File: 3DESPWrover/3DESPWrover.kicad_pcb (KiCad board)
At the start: 2 copper layers, 40 x 40 mm, 21 parts, among them J1 Conn_01x05_Male, J2 Conn_01x03_Female, J3 Conn_02x03_Odd_Even, J4 Conn_02x07_Odd_Even, SW1 SW_Push, SW2 SW_Push, U1 ESP32-S2-WROVER

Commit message: Cleared Andres comments
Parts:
- added NT1: Net-Tie_2, NetTie:NetTie-2_SMD_Pad0.5mm, B.Cu at (231.1, 85.5)
- added R4: 10k, Resistor_SMD:R_0805_2012Metric_Pad1.20x1.40mm_HandSolder, F.Cu at (211.5, 81.7)
- moved J4 0.97 mm to (232.8, 59.8)
- moved SW2 0.76 mm to (205.1, 79.1)
- moved J2 0.38 mm to (231.3, 81.2)
- turned C8 to 180 degrees
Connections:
- J3 pad 2: /D6 -> GND
- J3 pad 3: /Vin -> /D6
- J3 pad 5: GND -> /Vin
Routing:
- net /D14: track 47.4 -> 38.8 mm
- net /D15: track 44.7 -> 36.1 mm
- net /D16: track 46.2 -> 38.3 mm
- net /D13: track 42.3 -> 36.5 mm
- net /D12: track 43.7 -> 38.3 mm
- net /D11: track 39.4 -> 34.3 mm
- net /AD1: track 0.00 -> 5.12 mm, vias 0 -> 1
- net /D8: track 37.7 -> 33.1 mm
- net /D9: track 36.6 -> 32.1 mm
- net /D10: track 40.0 -> 36.2 mm
- net +3V3: track 79.1 -> 82.7 mm
- net GND: track 10.6 -> 7.31 mm
- net /D6: track 2.32 -> 5.36 mm
- net /NEOPIX: track 46.2 -> 48.5 mm
- net /RESET: track 19.8 -> 21.9 mm
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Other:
- outline, holes or cut-outs redrawn

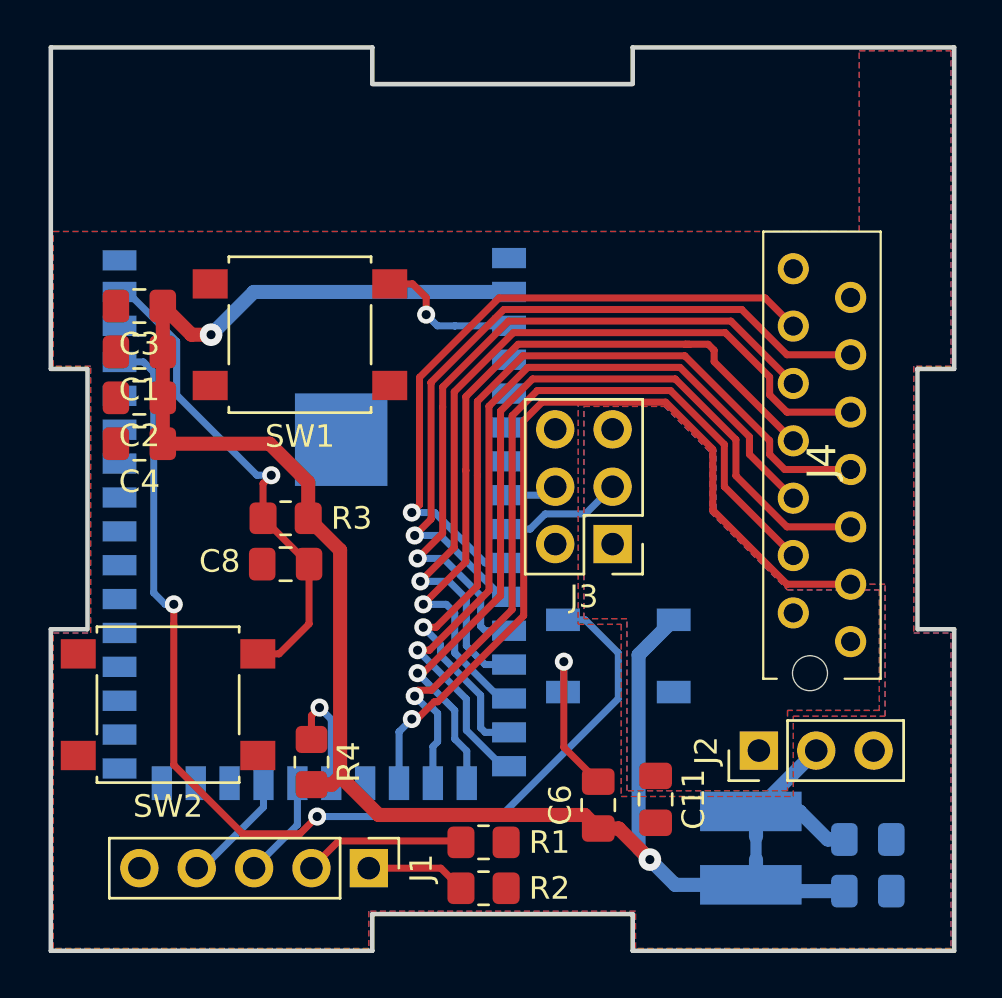
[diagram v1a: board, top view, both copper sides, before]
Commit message: Made corrections and added holes for zipties/nylon
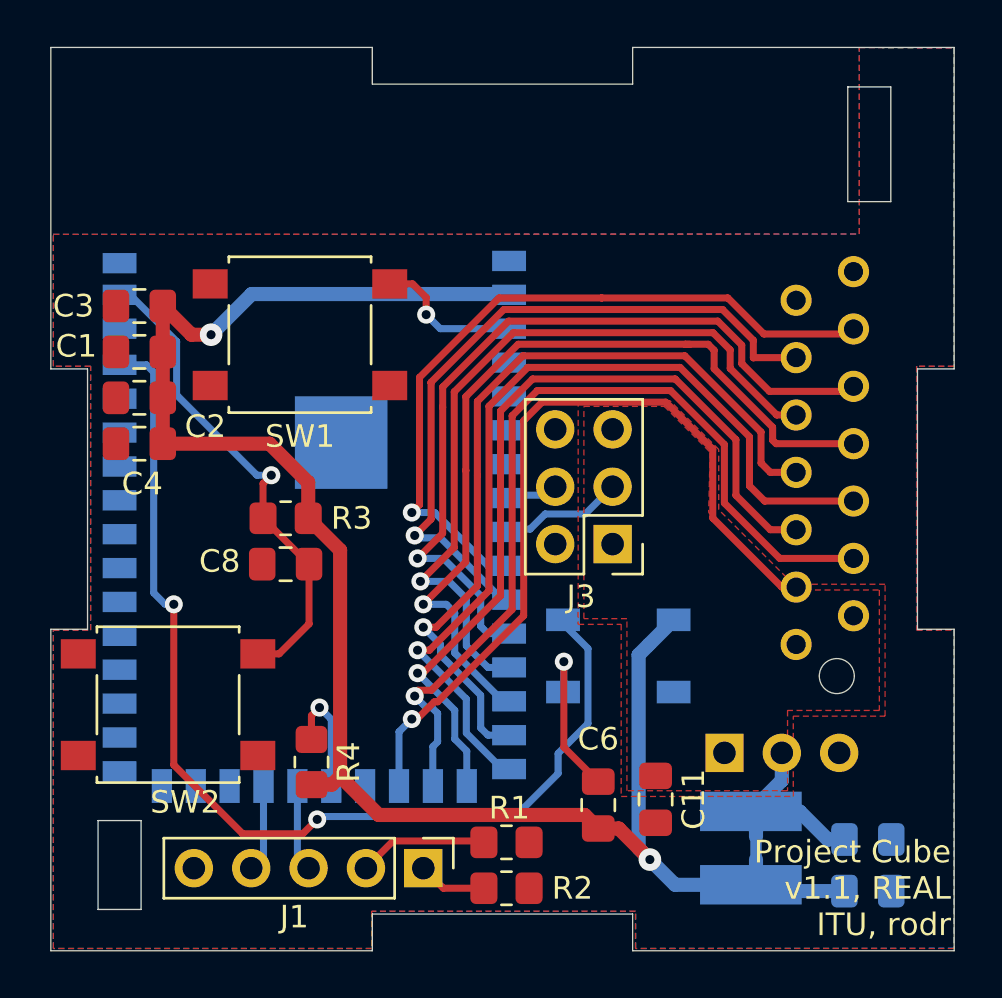
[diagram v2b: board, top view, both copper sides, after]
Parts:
- J2, J4: moved to B.Cu
- moved J4 2.67 mm to (235.5, 59.9)
- moved J1 2.41 mm to (216.4, 86.4)
- moved J2 1.53 mm to (229.7, 81.3), turned to 270 degrees
- moved R1 1.02 mm to (220.1, 85.2)
- moved R2 1.02 mm to (220.1, 87.2)
- moved U1 0.13 mm to (211.6, 71.2)
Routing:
- net /D13: track 36.5 -> 40.1 mm
- net /D9: track 32.1 -> 35.5 mm
- net /D11: track 34.3 -> 37.6 mm
- net /D15: track 36.1 -> 39.4 mm
- net /D7: track 29.9 -> 32.8 mm
- net /D10: track 36.2 -> 34.0 mm
- net /D12: track 38.3 -> 36.1 mm
- net /D16: track 38.3 -> 36.3 mm
- net /D14: track 38.8 -> 37.1 mm
- net /NEOPIX: track 48.5 -> 46.8 mm
- net /D8: track 33.1 -> 31.6 mm
- net Net-(J1-Pad2): track 7.15 -> 5.75 mm
- net Net-(J1-Pad1): track 4.45 -> 3.05 mm
- net /D+: track 5.14 -> 3.86 mm
- net /D-: track 4.56 -> 3.84 mm
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- removed copper zone on B.Cu, net /Vin
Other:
- outline, holes or cut-outs redrawn
- board text added: "Project Cube v1.1, REAL ITU, rodr"
